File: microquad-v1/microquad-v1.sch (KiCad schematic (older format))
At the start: 20 parts, among them M1 Motor_DC, M2 Motor_DC, M3 Motor_DC, M4 Motor_DC, M5 Motor_DC, M6 Motor_DC, Q1 Q_NMOS_DGS, Q2 Q_NMOS_DGS, Q3 Q_NMOS_DGS, Q4 Q_NMOS_DGS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

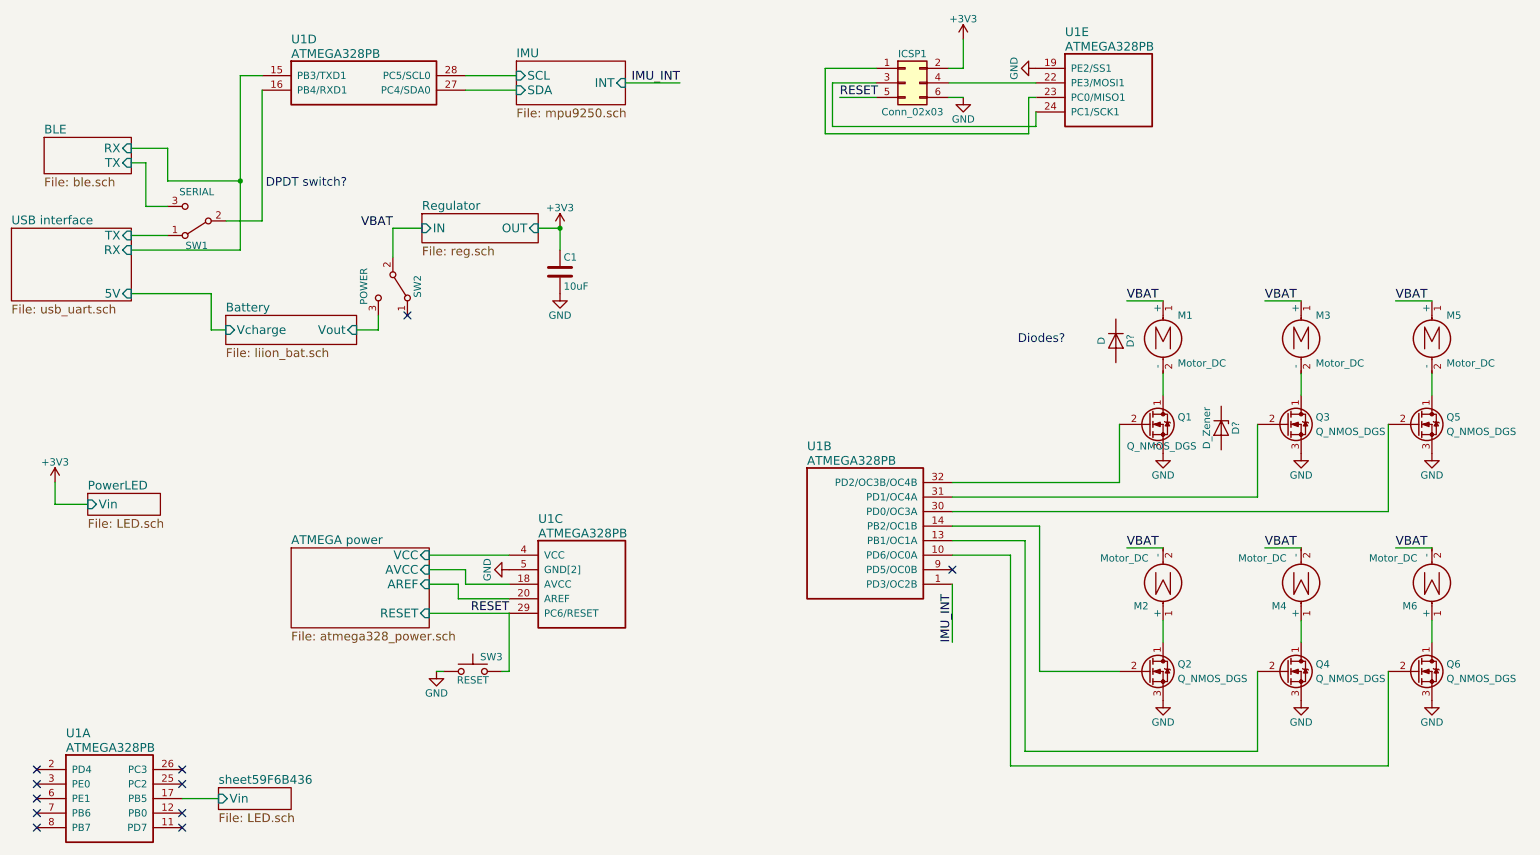
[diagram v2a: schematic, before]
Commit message: Changed to DPDT switches
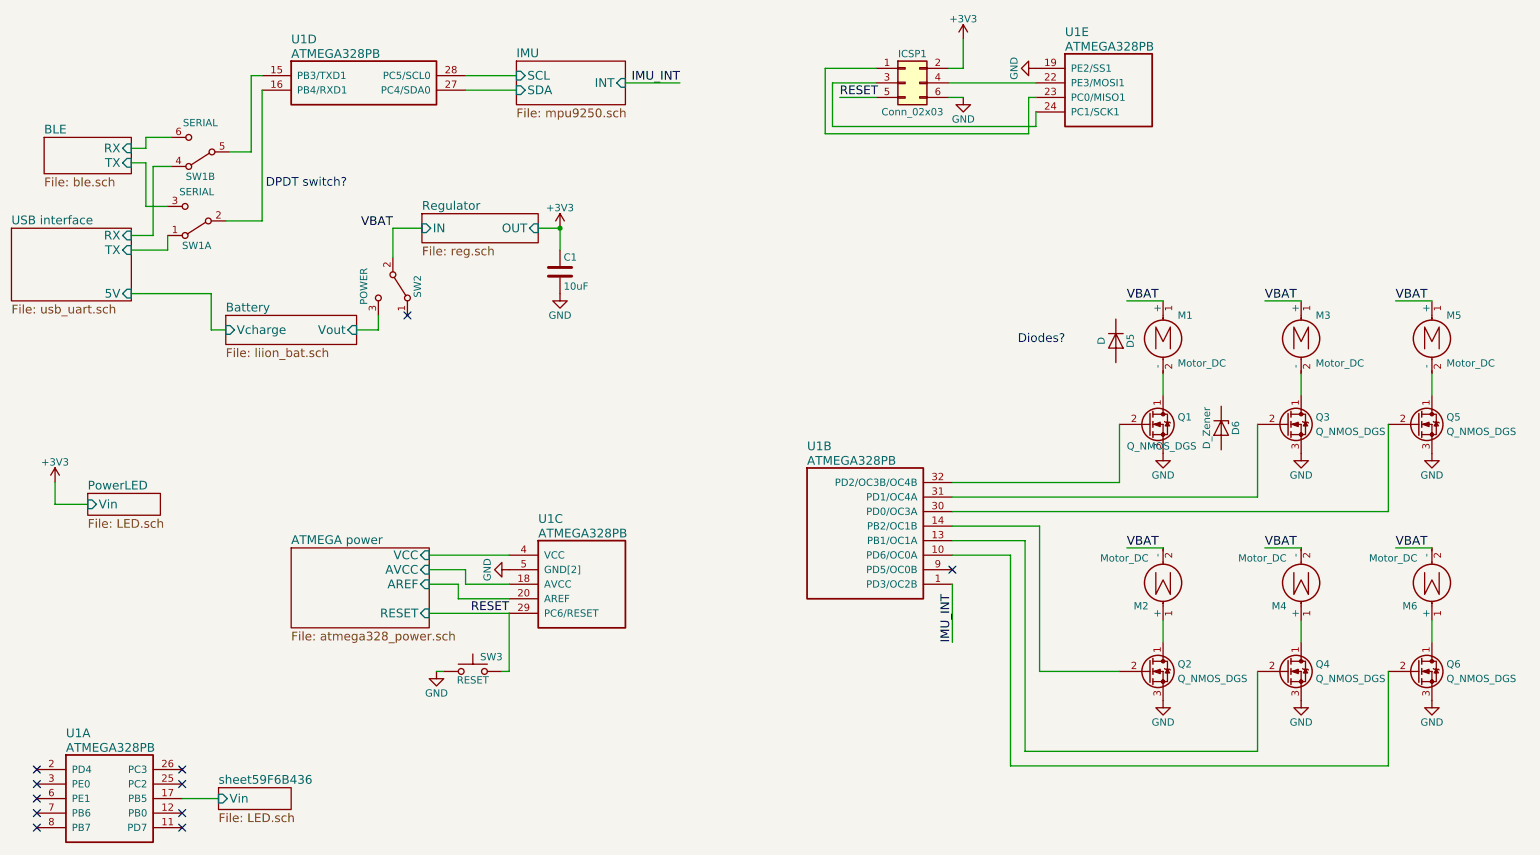
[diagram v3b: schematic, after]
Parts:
- removed SW1: SERIAL, symbol SW_SPDT
- added SW1: SERIAL, symbol SW_DPDT_x2
- gave numbers to parts that had none: 2
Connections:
- net BLE/RX: now also SW1.6 (C); no longer U1.15 (PB3/TXD1)
- net BLE/TX: now also SW1.3 (C)
- net USB interface/TX: now also SW1.1 (A)
- net at U1.16 (PB4/RXD1): now also SW1.2 (B)
- new net: SW1.5 (B), U1.15 (PB3/TXD1)
- new net USB interface/RX: SW1.4 (A)
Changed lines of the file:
@@
 F0 "USB interface" 60
 F1 "usb_uart.sch" 60
-F2 "RX" I R 1550 2450 60
-F3 "TX" I R 1550 2350 60
+F2 "RX" I R 1550 2350 60
+F3 "TX" I R 1550 2450 60
 F4 "5V" I R 1550 2750 60
 $EndSheet
@@
 	4150 4550 3600 4550
 $Comp
-L GND #PWR01
+L GND #PWR3
 U 1 1 59F2869E
 P 4150 4650
-F 0 "#PWR01" H 4150 4400 50  0001 C CNN
+F 0 "#PWR3" H 4150 4400 50  0001 C CNN
 F 1 "GND" H 4150 4500 50  0000 C CNN
 F 2 "" H 4150 4650 50  0001 C CNN
@@
 RESET
 $Comp
-L +3V3 #PWR02
+L +3V3 #PWR4
 U 1 1 59F530BC
 P 4500 2300
-F 0 "#PWR02" H 4500 2150 50  0001 C CNN
+F 0 "#PWR4" H 4500 2150 50  0001 C CNN
 F 1 "+3V3" H 4500 2440 50  0000 C CNN
 F 2 "" H 4500 2300 50  0001 C CNN
@@
 $EndComp
 $Comp
-L GND #PWR03
+L GND #PWR5
 U 1 1 59F54CA2
 P 4500 2750
-F 0 "#PWR03" H 4500 2500 50  0001 C CNN
+F 0 "#PWR5" H 4500 2500 50  0001 C CNN
 F 1 "GND" H 4500 2600 50  0000 C CNN
 F 2 "" H 4500 2750 50  0001 C CNN
@@
 $EndComp
 $Comp
-L GND #PWR04
+L GND #PWR9
 U 1 1 59F6C628
 P 8650 3850
-F 0 "#PWR04" H 8650 3600 50  0001 C CNN
+F 0 "#PWR9" H 8650 3600 50  0001 C CNN
 F 1 "GND" H 8650 3700 50  0000 C CNN
 F 2 "" H 8650 3850 50  0001 C CNN
@@
 $EndComp
 $Comp
-L GND #PWR05
+L GND #PWR11
 U 1 1 59F6F680
 P 9600 3850
-F 0 "#PWR05" H 9600 3600 50  0001 C CNN
+F 0 "#PWR11" H 9600 3600 50  0001 C CNN
 F 1 "GND" H 9600 3700 50  0000 C CNN
 F 2 "" H 9600 3850 50  0001 C CNN
@@
 $EndComp
 $Comp
-L GND #PWR06
+L GND #PWR13
 U 1 1 59F6F94E
 P 10500 3850
-F 0 "#PWR06" H 10500 3600 50  0001 C CNN
+F 0 "#PWR13" H 10500 3600 50  0001 C CNN
 F 1 "GND" H 10500 3700 50  0000 C CNN
 F 2 "" H 10500 3850 50  0001 C CNN
@@
 $EndComp
 $Comp
-L GND #PWR07
+L GND #PWR10
 U 1 1 59F700FC
 P 8650 5550
-F 0 "#PWR07" H 8650 5300 50  0001 C CNN
+F 0 "#PWR10" H 8650 5300 50  0001 C CNN
 F 1 "GND" H 8650 5400 50  0000 C CNN
 F 2 "" H 8650 5550 50  0001 C CNN
@@
 $EndComp
 $Comp
-L GND #PWR08
+L GND #PWR12
 U 1 1 59F70111
 P 9600 5550
-F 0 "#PWR08" H 9600 5300 50  0001 C CNN
+F 0 "#PWR12" H 9600 5300 50  0001 C CNN
 F 1 "GND" H 9600 5400 50  0000 C CNN
 F 2 "" H 9600 5550 50  0001 C CNN
@@
 $EndComp
 $Comp
-L GND #PWR09
+L GND #PWR14
 U 1 1 59F70128
 P 10500 5550
-F 0 "#PWR09" H 10500 5300 50  0001 C CNN
+F 0 "#PWR14" H 10500 5300 50  0001 C CNN
 F 1 "GND" H 10500 5400 50  0000 C CNN
 F 2 "" H 10500 5550 50  0001 C CNN
@@
 	1650 2150 1800 2150
 Wire Wire Line
-	1800 1750 1800 1975
-Wire Wire Line
-	1800 1975 2300 1975
-Wire Wire Line
-	2300 1250 2300 2450
-Wire Wire Line
-	2300 1250 2450 1250
-Wire Wire Line
 	2450 2250 2450 1350
 Wire Wire Line
 	2200 2250 2450 2250
-Wire Wire Line
-	1800 2350 1550 2350
-Wire Wire Line
-	2300 2450 1550 2450
-Connection ~ 2300 1975
 $Sheet
 S 1250 4125 500  150
@@
 $EndSheet
 $Comp
-L +3V3 #PWR010
+L +3V3 #PWR1
 U 1 1 59F6B9F3
 P 1025 4050
-F 0 "#PWR010" H 1025 3900 50  0001 C CNN
+F 0 "#PWR1" H 1025 3900 50  0001 C CNN
 F 1 "+3V3" H 1025 4190 50  0000 C CNN
 F 2 "" H 1025 4050 50  0001 C CNN
@@
 $EndComp
 $Comp
-L GND #PWR011
+L GND #PWR2
 U 1 1 59F7EFD3
 P 3650 5350
-F 0 "#PWR011" H 3650 5100 50  0001 C CNN
+F 0 "#PWR2" H 3650 5100 50  0001 C CNN
 F 1 "GND" H 3650 5200 50  0000 C CNN
 F 2 "" H 3650 5350 50  0001 C CNN
@@
 	7175 1400 7275 1400
 $Comp
-L GND #PWR012
+L GND #PWR7
 U 1 1 59F8679D
 P 7275 1400
-F 0 "#PWR012" H 7275 1150 50  0001 C CNN
+F 0 "#PWR7" H 7275 1150 50  0001 C CNN
 F 1 "GND" H 7275 1250 50  0000 C CNN
 F 2 "" H 7275 1400 50  0001 C CNN
@@
 RESET
 $Comp
-L GND #PWR013
+L GND #PWR8
 U 1 1 59F8B068
 P 7775 1200
-F 0 "#PWR013" H 7775 950 50  0001 C CNN
+F 0 "#PWR8" H 7775 950 50  0001 C CNN
 F 1 "GND" H 7775 1050 50  0000 C CNN
 F 2 "" H 7775 1200 50  0001 C CNN
@@
 	0    1    1    0
 $EndComp
-$Comp
-L SW_SPDT SW1
-U 1 1 59F9E9A3
-P 2000 2250
-F 0 "SW1" H 2000 2420 50  0000 C CNN
-F 1 "SERIAL" H 2000 2050 50  0000 C CNN
-F 2 "" H 2000 2250 50  0001 C CNN
-F 3 "" H 2000 2250 50  0001 C CNN
-	1    2000 2250
-	-1   0    0    1
-$EndComp
 Connection ~ 4500 2300
-Wire Wire Line
-	1800 1750 1550 1750
 $Sheet
 S 950  1675 600  250
@@
 Diodes?
 $Comp
-L D D?
+L D D5
 U 1 1 59F7DE54
 P 8325 3075
-F 0 "D?" H 8325 3175 50  0000 C CNN
+F 0 "D5" H 8325 3175 50  0000 C CNN
 F 1 "D" H 8325 2975 50  0000 C CNN
 F 2 "" H 8325 3075 50  0001 C CNN
@@
 DPDT switch?\n
 $Comp
-L +3V3 #PWR?
+L +3V3 #PWR6
 U 1 1 59F86353
 P 7275 1000
-F 0 "#PWR?" H 7275 850 50  0001 C CNN
+F 0 "#PWR6" H 7275 850 50  0001 C CNN
 F 1 "+3V3" H 7275 1140 50  0000 C CNN
 F 2 "" H 7275 1000 50  0001 C CNN
@@
 $EndComp
 $Comp
-L D_Zener D?
+L D_Zener D6
 U 1 1 59F87D4C
 P 9050 3675
-F 0 "D?" H 9050 3775 50  0000 C CNN
+F 0 "D6" H 9050 3775 50  0000 C CNN
 F 1 "D_Zener" H 9050 3575 50  0000 C CNN
 F 2 "" H 9050 3675 50  0001 C CNN
@@
 	0    1    1    0
 $EndComp
+$Comp
+L SW_DPDT_x2 SW1
+U 1 1 59F7AC4E
+P 2000 2250
+F 0 "SW1" H 2000 2420 50  0000 C CNN
+F 1 "SERIAL" H 2000 2050 50  0000 C CNN
+F 2 "" H 2000 2250 50  0001 C CNN
+F 3 "" H 2000 2250 50  0001 C CNN
+	1    2000 2250
+	-1   0    0    1
+$EndComp
+$Comp
+L SW_DPDT_x2 SW1
+U 2 1 59F7AD73
+P 2025 1775
+F 0 "SW1" H 2025 1945 50  0000 C CNN
+F 1 "SERIAL" H 2025 1575 50  0000 C CNN
+F 2 "" H 2025 1775 50  0001 C CNN
+F 3 "" H 2025 1775 50  0001 C CNN
+	2    2025 1775
+	-1   0    0    1
+$EndComp
+Wire Wire Line
+	1550 1750 1650 1750
+Wire Wire Line
+	1650 1750 1650 1675
+Wire Wire Line
+	1650 1675 1825 1675
+Wire Wire Line
+	1825 1875 1700 1875
+Wire Wire Line
+	2225 1775 2375 1775
+Wire Wire Line
+	2375 1775 2375 1250
+Wire Wire Line
+	2375 1250 2450 1250
+Wire Wire Line
+	1550 2350 1700 2350
+Wire Wire Line
+	1700 2350 1700 1875
+Wire Wire Line
+	1800 2350 1800 2450
+Wire Wire Line
+	1800 2450 1550 2450
 $EndSCHEMATC

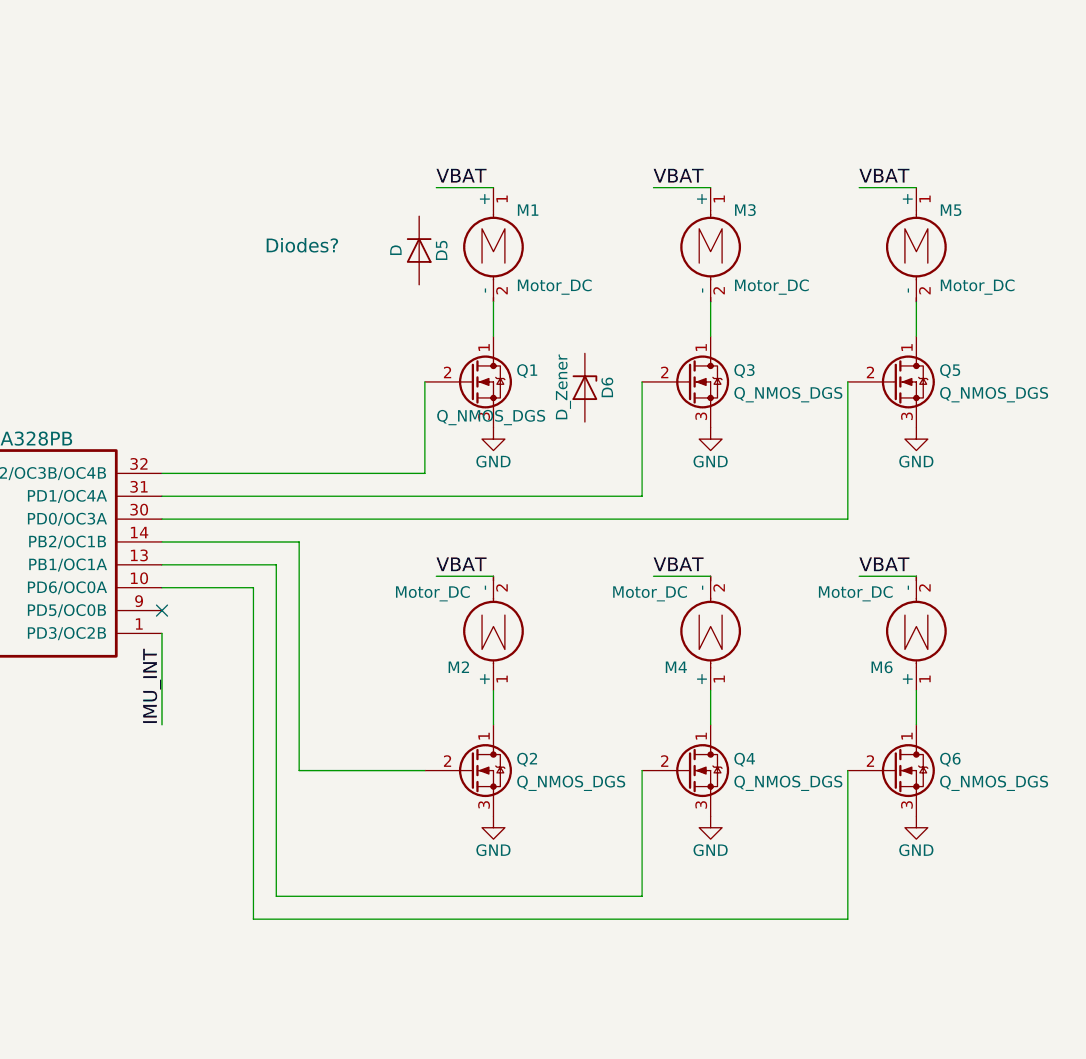
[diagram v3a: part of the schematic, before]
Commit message: Added bypass diodes and extracted motors into separate schematic
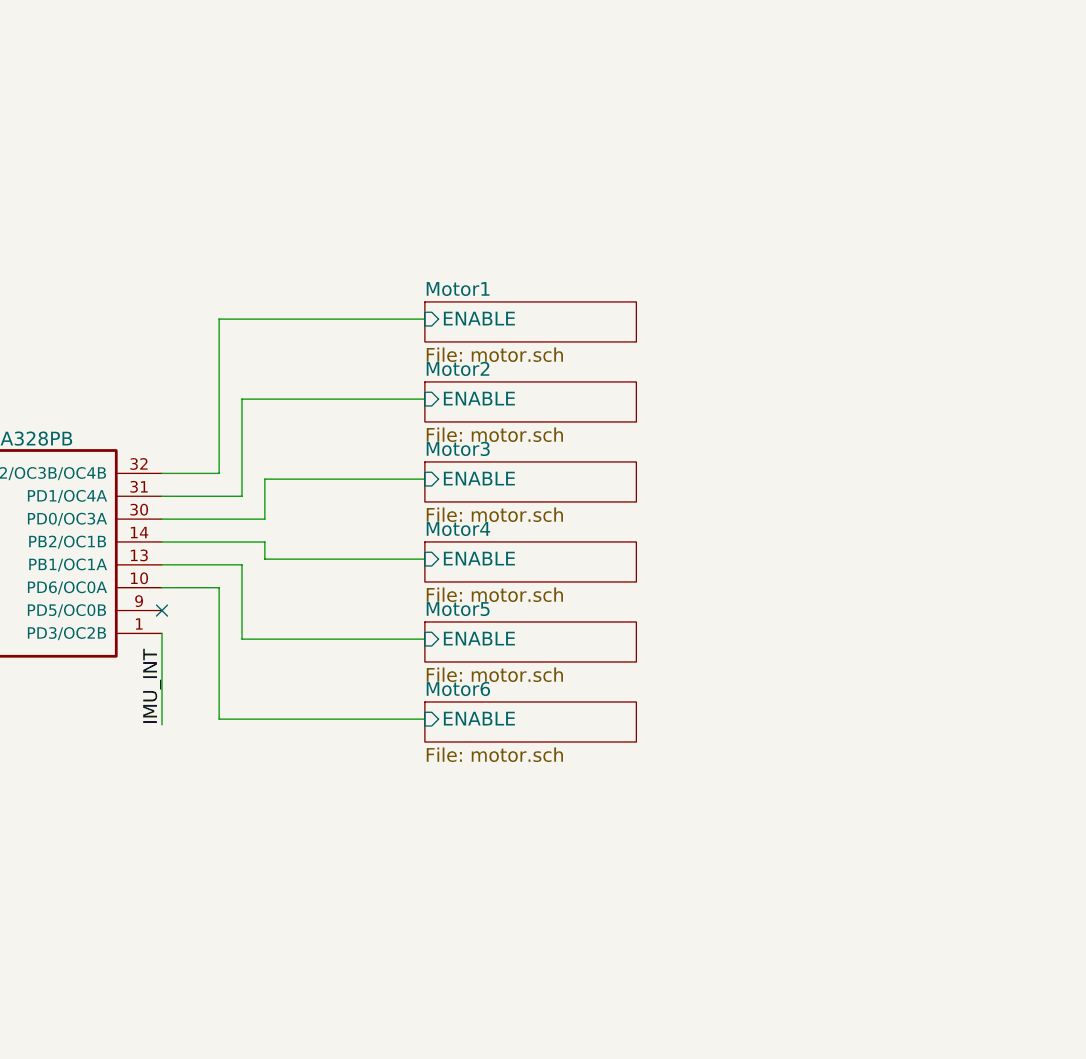
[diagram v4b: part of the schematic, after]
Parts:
- removed D5: D, symbol D
- removed D6: D_Zener, symbol D_Zener
- removed M1, M2, M3, M4, M5, M6: Motor_DC, symbol Motor_DC
- removed Q1, Q2, Q3, Q4, Q5, Q6: Q_NMOS_DGS, symbol Q_NMOS_DGS
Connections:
- net Motor6/ENABLE: now reaches U1.10 (PD6/OC0A)
- net Motor5/ENABLE: now reaches U1.13 (PB1/OC1A)
- net Motor4/ENABLE: now reaches U1.14 (PB2/OC1B)
- net Motor3/ENABLE: now reaches U1.30 (PD0/OC3A)
- net Motor2/ENABLE: now reaches U1.31 (PD1/OC4A)
- net Motor1/ENABLE: now reaches U1.32 (PD2/OC3B/OC4B)
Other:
- note removed: "Diodes?"

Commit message: Added layout for transistor
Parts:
- ICSP1: footprint (none) -> Pin_Headers:Pin_Header_Straight_2x03_Pitch2.54mm
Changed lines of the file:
@@
 	4150 4550 3600 4550
 $Comp
-L GND #PWR3
+L GND #PWR01
 U 1 1 59F2869E
 P 4150 4650
-F 0 "#PWR3" H 4150 4400 50  0001 C CNN
+F 0 "#PWR01" H 4150 4400 50  0001 C CNN
 F 1 "GND" H 4150 4500 50  0000 C CNN
 F 2 "" H 4150 4650 50  0001 C CNN
@@
 RESET
 $Comp
-L +3V3 #PWR4
+L +3V3 #PWR02
 U 1 1 59F530BC
 P 4500 2300
-F 0 "#PWR4" H 4500 2150 50  0001 C CNN
+F 0 "#PWR02" H 4500 2150 50  0001 C CNN
 F 1 "+3V3" H 4500 2440 50  0000 C CNN
 F 2 "" H 4500 2300 50  0001 C CNN
@@
 $EndComp
 $Comp
-L GND #PWR5
+L GND #PWR03
 U 1 1 59F54CA2
 P 4500 2750
-F 0 "#PWR5" H 4500 2500 50  0001 C CNN
+F 0 "#PWR03" H 4500 2500 50  0001 C CNN
 F 1 "GND" H 4500 2600 50  0000 C CNN
 F 2 "" H 4500 2750 50  0001 C CNN
@@
 $EndSheet
 $Comp
-L +3V3 #PWR1
+L +3V3 #PWR04
 U 1 1 59F6B9F3
 P 1025 4050
-F 0 "#PWR1" H 1025 3900 50  0001 C CNN
+F 0 "#PWR04" H 1025 3900 50  0001 C CNN
 F 1 "+3V3" H 1025 4190 50  0000 C CNN
 F 2 "" H 1025 4050 50  0001 C CNN
@@
 $EndComp
 $Comp
-L GND #PWR2
+L GND #PWR05
 U 1 1 59F7EFD3
 P 3650 5350
-F 0 "#PWR2" H 3650 5100 50  0001 C CNN
+F 0 "#PWR05" H 3650 5100 50  0001 C CNN
 F 1 "GND" H 3650 5200 50  0000 C CNN
 F 2 "" H 3650 5350 50  0001 C CNN
@@
 F 0 "ICSP1" H 6925 1500 50  0000 C CNN
 F 1 "Conn_02x03" H 6925 1100 50  0000 C CNN
-F 2 "" H 6875 1300 50  0001 C CNN
+F 2 "Pin_Headers:Pin_Header_Straight_2x03_Pitch2.54mm" H 6875 1300 50  0001 C CNN
 F 3 "" H 6875 1300 50  0001 C CNN
 	1    6875 1300
@@
 	7175 1400 7275 1400
 $Comp
-L GND #PWR7
+L GND #PWR06
 U 1 1 59F8679D
 P 7275 1400
-F 0 "#PWR7" H 7275 1150 50  0001 C CNN
+F 0 "#PWR06" H 7275 1150 50  0001 C CNN
 F 1 "GND" H 7275 1250 50  0000 C CNN
 F 2 "" H 7275 1400 50  0001 C CNN
@@
 RESET
 $Comp
-L GND #PWR8
+L GND #PWR07
 U 1 1 59F8B068
 P 7775 1200
-F 0 "#PWR8" H 7775 950 50  0001 C CNN
+F 0 "#PWR07" H 7775 950 50  0001 C CNN
 F 1 "GND" H 7775 1050 50  0000 C CNN
 F 2 "" H 7775 1200 50  0001 C CNN
@@
 DPDT switch?\n
 $Comp
-L +3V3 #PWR6
+L +3V3 #PWR08
 U 1 1 59F86353
 P 7275 1000
-F 0 "#PWR6" H 7275 850 50  0001 C CNN
+F 0 "#PWR08" H 7275 850 50  0001 C CNN
 F 1 "+3V3" H 7275 1140 50  0000 C CNN
 F 2 "" H 7275 1000 50  0001 C CNN

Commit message: Finished footprint work 10/31
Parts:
- SW1, SW2: footprint (none) -> motor:quad_switch
- SW3: footprint (none) -> Buttons_Switches_SMD:SW_SPST_B3U-1000P
- U1: footprint (none) -> Housings_QFP:TQFP-32_7x7mm_Pitch0.8mm
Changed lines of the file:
@@
 F 0 "U1" H 6200 4300 60  0000 L CNN
 F 1 "ATMEGA328PB" H 6200 4200 60  0000 L CNN
-F 2 "" H 6000 4050 60  0001 C CNN
+F 2 "Housings_QFP:TQFP-32_7x7mm_Pitch0.8mm" H 6000 4050 60  0001 C CNN
 F 3 "" H 6000 4050 60  0001 C CNN
 	2    6000 4050
@@
 F 0 "U1" H 1100 6275 60  0000 L CNN
 F 1 "ATMEGA328PB" H 1100 6175 60  0000 L CNN
-F 2 "" H 900 6025 60  0001 C CNN
+F 2 "Housings_QFP:TQFP-32_7x7mm_Pitch0.8mm" H 900 6025 60  0001 C CNN
 F 3 "" H 900 6025 60  0001 C CNN
 	1    900  6025
@@
 F 0 "U1" H 4350 4800 60  0000 L CNN
 F 1 "ATMEGA328PB" H 4350 4700 60  0000 L CNN
-F 2 "" H 4150 4550 60  0001 C CNN
+F 2 "Housings_QFP:TQFP-32_7x7mm_Pitch0.8mm" H 4150 4550 60  0001 C CNN
 F 3 "" H 4150 4550 60  0001 C CNN
 	3    4150 4550
@@
 F 0 "U1" H 2650 1500 60  0000 L CNN
 F 1 "ATMEGA328PB" H 2650 1400 60  0000 L CNN
-F 2 "" H 2450 1250 60  0001 C CNN
+F 2 "Housings_QFP:TQFP-32_7x7mm_Pitch0.8mm" H 2450 1250 60  0001 C CNN
 F 3 "" H 2450 1250 60  0001 C CNN
 	4    2450 1250
@@
 F 0 "U1" H 7975 1450 60  0000 L CNN
 F 1 "ATMEGA328PB" H 7975 1350 60  0000 L CNN
-F 2 "" H 7775 1200 60  0001 C CNN
+F 2 "Housings_QFP:TQFP-32_7x7mm_Pitch0.8mm" H 7775 1200 60  0001 C CNN
 F 3 "" H 7775 1200 60  0001 C CNN
 	5    7775 1200
@@
 F 0 "SW3" H 3950 5450 50  0000 L CNN
 F 1 "RESET" H 3900 5290 50  0000 C CNN
-F 2 "" H 3900 5550 50  0001 C CNN
+F 2 "Buttons_Switches_SMD:SW_SPST_B3U-1000P" H 3900 5550 50  0001 C CNN
 F 3 "" H 3900 5550 50  0001 C CNN
 	1    3900 5350
@@
 F 0 "SW2" H 3350 2870 50  0000 C CNN
 F 1 "POWER" H 3350 2500 50  0000 C CNN
-F 2 "" H 3350 2700 50  0001 C CNN
+F 2 "motor:quad_switch" H 3350 2700 50  0001 C CNN
 F 3 "" H 3350 2700 50  0001 C CNN
 	1    3350 2700
@@
 F 0 "SW1" H 2000 2420 50  0000 C CNN
 F 1 "SERIAL" H 2000 2050 50  0000 C CNN
-F 2 "" H 2000 2250 50  0001 C CNN
+F 2 "motor:quad_switch" H 2000 2250 50  0001 C CNN
 F 3 "" H 2000 2250 50  0001 C CNN
 	1    2000 2250
@@
 F 0 "SW1" H 2025 1945 50  0000 C CNN
 F 1 "SERIAL" H 2025 1575 50  0000 C CNN
-F 2 "" H 2025 1775 50  0001 C CNN
+F 2 "motor:quad_switch" H 2025 1775 50  0001 C CNN
 F 3 "" H 2025 1775 50  0001 C CNN
 	2    2025 1775
